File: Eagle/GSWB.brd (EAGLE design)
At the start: 41.1 x 53.3 mm, 14 parts

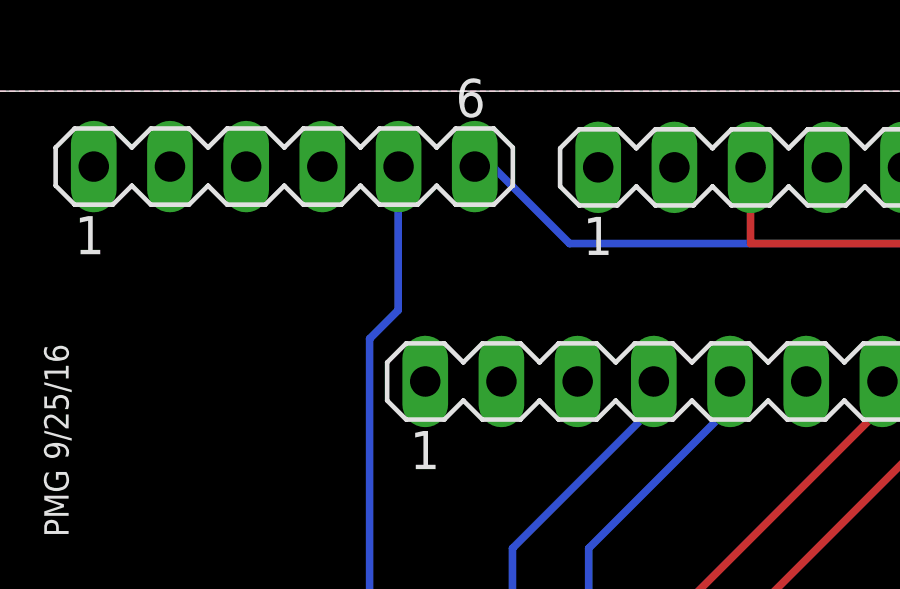
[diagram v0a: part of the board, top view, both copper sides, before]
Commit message: updated Gerber files
Added trace from lbat to D10
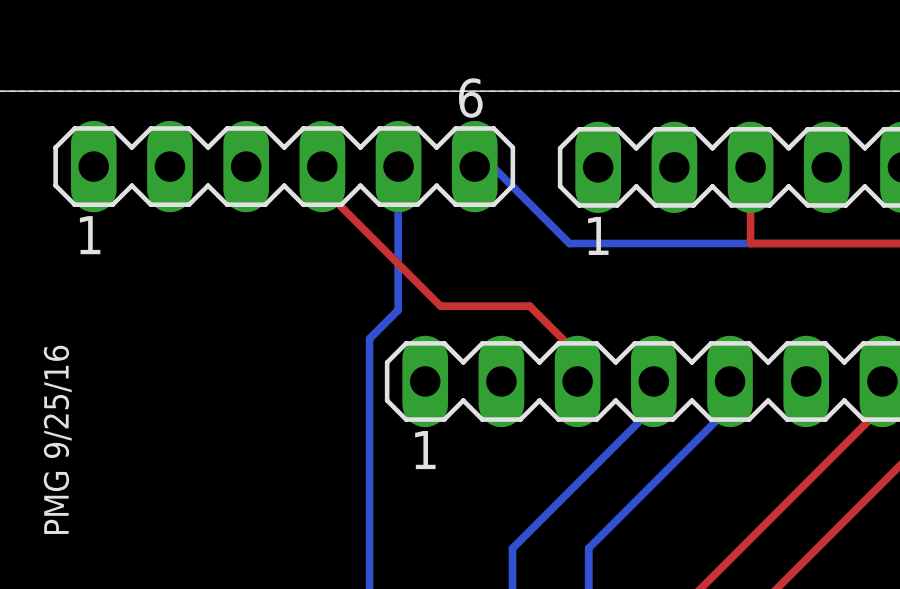
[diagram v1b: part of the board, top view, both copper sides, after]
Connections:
- new net N$15: SV5.3, SV8.4
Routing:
- net N$15: track 0.00 -> 12.4 mm
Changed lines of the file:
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@@
 <wire x1="19.939" y1="10.16" x2="19.812" y2="9.906" width="0.254" layer="1"/>
+</signal>
+<signal name="N$15">
+<contactref element="SV5" pad="3"/>
+<contactref element="SV8" pad="4"/>
+<wire x1="11.43" y1="50.0634" x2="11.43" y2="50.7492" width="0.254" layer="1"/>
+<wire x1="15.3162" y1="46.1772" x2="11.43" y2="50.0634" width="0.254" layer="1"/>
+<wire x1="18.288" y1="46.1772" x2="15.3162" y2="46.1772" width="0.254" layer="1"/>
+<wire x1="19.8882" y1="44.577" x2="18.288" y2="46.1772" width="0.254" layer="1"/>
+<wire x1="19.8882" y1="43.6626" x2="19.8882" y2="44.577" width="0.254" layer="1"/>
+<wire x1="11.43" y1="50.7492" x2="11.3792" y2="50.8254" width="0.254" layer="1"/>
 </signal>
 </signals>

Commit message: Adding CAD Files
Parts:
- R4: value RC1206FR-07100RL -> RT1210BRD07150RL
- moved SV6 0.76 mm to (32.8, 10.7)
- moved SV7 0.76 mm to (16.0, 10.7)
- moved SV5 0.48 mm to (23.5, 43.2), turned to 180 degrees
- turned JP2 to 270 degrees
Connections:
- net EN_GND: now also SV5.1
- net GND: now also SV2.3, SV5.2
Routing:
- net EN_GND: track 29.1 -> 69.1 mm
- net SW5V: track 46.9 -> 61.6 mm, vias 1 -> 0
- net N$2: track 27.5 -> 36.4 mm
- net N$13: track 36.6 -> 28.8 mm
- net N$15: track 12.4 -> 19.2 mm
- net N$1: track 31.5 -> 25.7 mm
- net N$10: track 30.2 -> 25.6 mm
- net N$7: track 26.2 -> 29.7 mm, vias 0 -> 1
- net N$4: track 47.3 -> 44.9 mm, vias 1 -> 0
- net N$14: track 18.4 -> 16.8 mm, vias 0 -> 1
- net GND: track 0.00 -> 1.55 mm, vias 0 -> 1
- net N$9: track 7.63 -> 8.42 mm
- net N$11: track 7.63 -> 8.42 mm
- net N$12: track 8.23 -> 9.02 mm
- net N$6: track 39.5 -> 38.9 mm
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- removed copper zone on layer 1, net GND
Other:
- board text added: "GSWB V2.0.2"
- board text added: "PMG 10/1/16"
- board text added: "R1= 10K R2= 100 R3= 100 R4= 150"
- board text removed: "GSWB V1.0.0"
- board text removed: "PMG 9/25/16"
